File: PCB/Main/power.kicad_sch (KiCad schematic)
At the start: 6 parts

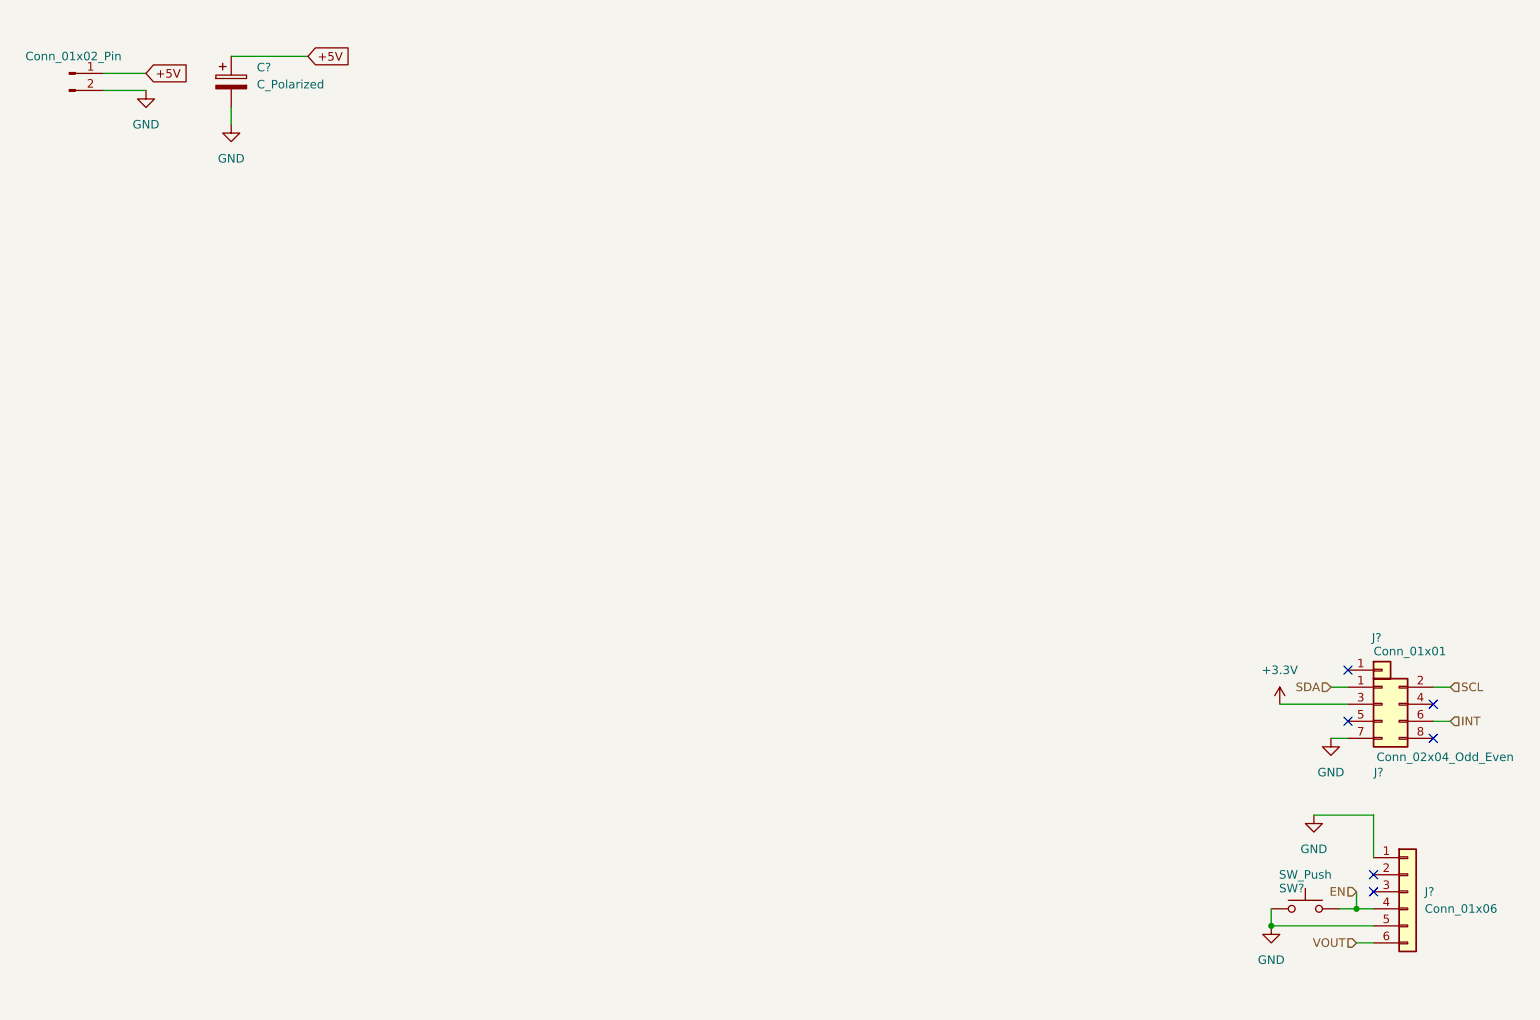
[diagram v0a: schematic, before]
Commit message: renaming y basico sin pcb
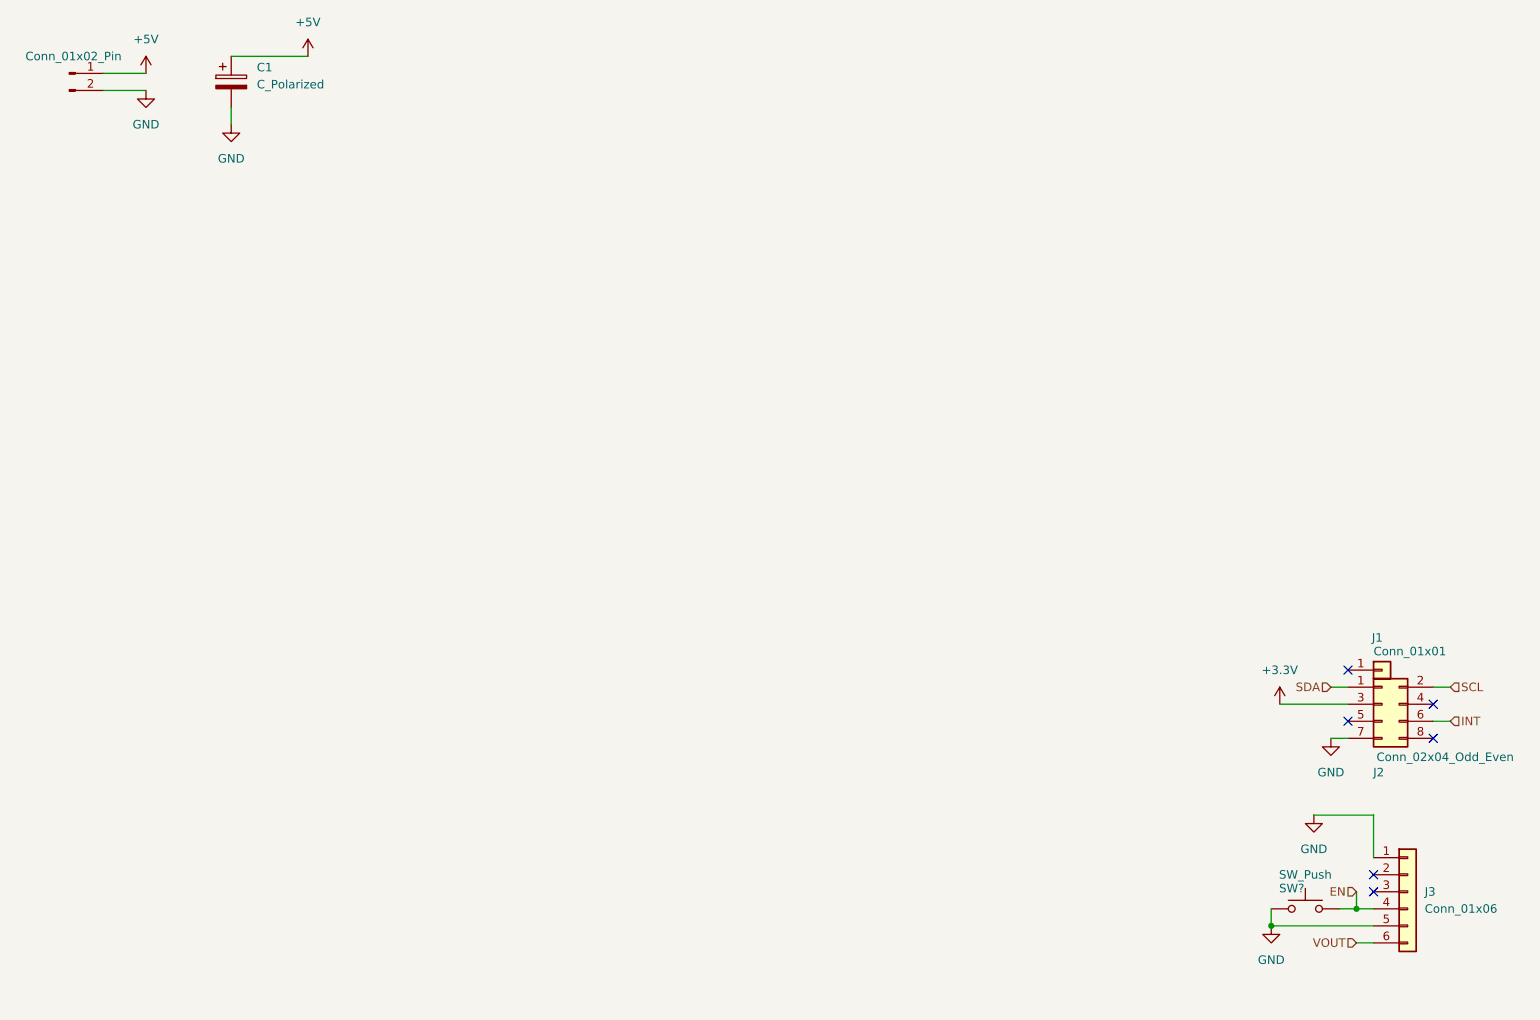
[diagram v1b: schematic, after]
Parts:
- gave numbers to parts that had none: 4
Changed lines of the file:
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@@
-		)
-	)
-	(global_label "+5V"
-		(shape input)
-		(at 68.58 24.13 0)
-		(fields_autoplaced yes)
-		(effects
-			(font
-				(size 1.27 1.27)
-			)
-			(justify left)
-		)
-		(property "Intersheetrefs" "${INTERSHEET_REFS}"
-			(at 75.4357 24.13 0)
-			(effects
-				(font
-					(size 1.27 1.27)
-				)
-				(justify left)
-				(hide yes)
-			)
-		)
-	)
-	(global_label "+5V"
-		(shape input)
-		(at 44.45 26.67 0)
-		(fields_autoplaced yes)
-		(effects
-			(font
-				(size 1.27 1.27)
-			)
-			(justify left)
-		)
-		(property "Intersheetrefs" "${INTERSHEET_REFS}"
-			(at 51.3057 26.67 0)
-			(effects
-				(font
-					(size 1.27 1.27)
-				)
-				(justify left)
-				(hide yes)
-			)
 		)
 	)
@@
 		(dnp no)
 		(fields_autoplaced yes)
-		(property "Reference" "J?"
+		(property "Reference" "J3"
 			(at 234.95 148.5899 0)
 			(effects
@@
 			(project "Main"
 				(path "/dea5ac8e-3e86-4300-9e2e-2676721051d5/57741c9e-edd5-4d78-9bed-1b543f87d51f"
-					(reference "J?")
+					(reference "J3")
+					(unit 1)
+				)
+			)
+		)
+	)
+	(symbol
+		(lib_id "power:+5V")
+		(at 44.45 26.67 0)
+		(unit 1)
+		(exclude_from_sim no)
+		(in_bom yes)
+		(on_board yes)
+		(dnp no)
+		(fields_autoplaced yes)
+		(property "Reference" "#PWR05"
+			(at 44.45 30.48 0)
+			(effects
+				(font
+					(size 1.27 1.27)
+				)
+				(hide yes)
+			)
+		)
+		(property "Value" "+5V"
+			(at 44.45 21.59 0)
+			(effects
+				(font
+					(size 1.27 1.27)
+				)
+			)
+		)
+		(property "Footprint" ""
+			(at 44.45 26.67 0)
+			(effects
+				(font
+					(size 1.27 1.27)
+				)
+				(hide yes)
+			)
+		)
+		(property "Datasheet" ""
+			(at 44.45 26.67 0)
+			(effects
+				(font
+					(size 1.27 1.27)
+				)
+				(hide yes)
+			)
+		)
+		(property "Description" "Power symbol creates a global label with name \"+5V\""
+			(at 44.45 26.67 0)
+			(effects
+				(font
+					(size 1.27 1.27)
+				)
+				(hide yes)
+			)
+		)
+		(pin "1"
+		)
+		(instances
+			(project ""
+				(path "/dea5ac8e-3e86-4300-9e2e-2676721051d5/57741c9e-edd5-4d78-9bed-1b543f87d51f"
+					(reference "#PWR05")
 					(unit 1)
 				)
@@
 		(dnp no)
 		(fields_autoplaced yes)
-		(property "Reference" "C?"
+		(property "Reference" "C1"
 			(at 60.96 25.7809 0)
 			(effects
@@
 			(project "Main"
 				(path "/dea5ac8e-3e86-4300-9e2e-2676721051d5/57741c9e-edd5-4d78-9bed-1b543f87d51f"
-					(reference "C?")
+					(reference "C1")
 					(unit 1)
 				)
@@
 		(on_board yes)
 		(dnp no)
-		(property "Reference" "J?"
+		(property "Reference" "J2"
 			(at 228.092 130.81 0)
 			(effects
@@
 			(project "Main"
 				(path "/dea5ac8e-3e86-4300-9e2e-2676721051d5/57741c9e-edd5-4d78-9bed-1b543f87d51f"
-					(reference "J?")
+					(reference "J2")
 					(unit 1)
 				)
@@
 		(on_board yes)
 		(dnp no)
-		(property "Reference" "J?"
+		(property "Reference" "J1"
 			(at 227.076 110.744 0)
 			(effects
@@
 			(project "Main"
 				(path "/dea5ac8e-3e86-4300-9e2e-2676721051d5/57741c9e-edd5-4d78-9bed-1b543f87d51f"
-					(reference "J?")
+					(reference "J1")
 					(unit 1)
 				)
@@
 					(unit 1)
 				)
+			)
+		)
+	)
+	(symbol
+		(lib_id "power:+5V")
+		(at 68.58 24.13 0)
+		(unit 1)
+		(exclude_from_sim no)
+		(in_bom yes)
+		(on_board yes)
+		(dnp no)
+		(fields_autoplaced yes)
+		(property "Reference" "#PWR06"
+			(at 68.58 27.94 0)
+			(effects
+				(font
+					(size 1.27 1.27)
+				)
+				(hide yes)
+			)
+		)
+		(property "Value" "+5V"
+			(at 68.58 19.05 0)
+			(effects
+				(font
+					(size 1.27 1.27)
+				)
+			)
+		)
+		(property "Footprint" ""
+			(at 68.58 24.13 0)
+			(effects
+				(font
+					(size 1.27 1.27)
+				)
+				(hide yes)
+			)
+		)
+		(property "Datasheet" ""
+			(at 68.58 24.13 0)
+			(effects
+				(font
+					(size 1.27 1.27)
+				)
+				(hide yes)
+			)
+		)
+		(property "Description" "Power symbol creates a global label with name \"+5V\""
+			(at 68.58 24.13 0)
+			(effects
+				(font
+					(size 1.27 1.27)
+				)
+				(hide yes)
+			)
+		)
+		(pin "1"
+		)
+		(instances
+			(project ""
+				(path "/dea5ac8e-3e86-4300-9e2e-2676721051d5/57741c9e-edd5-4d78-9bed-1b543f87d51f"
+					(reference "#PWR06")
+					(unit 1)
+				)

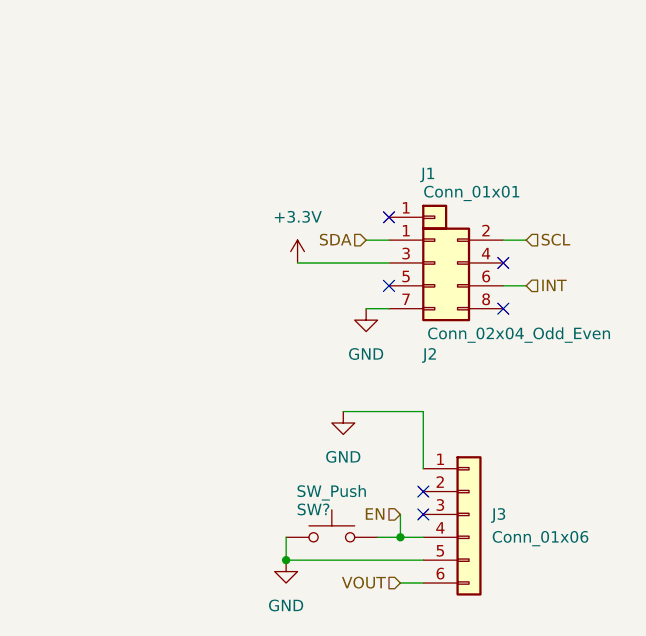
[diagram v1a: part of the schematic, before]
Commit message: rename y conectores
tambien se añaden pours
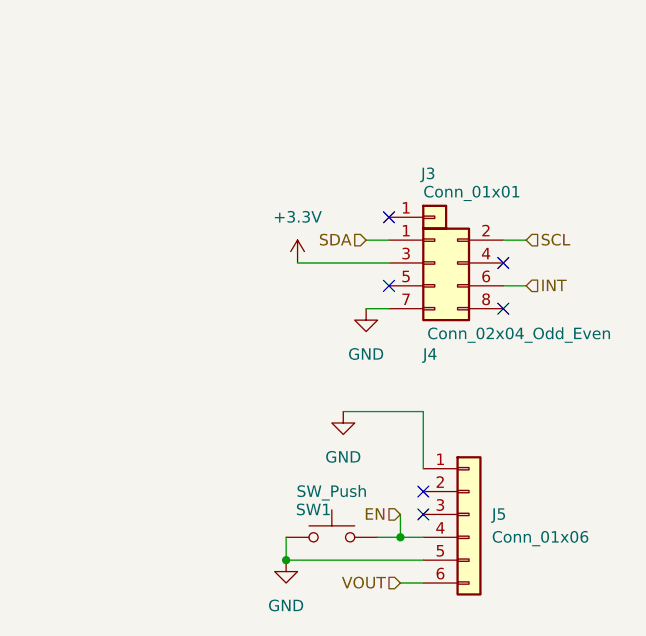
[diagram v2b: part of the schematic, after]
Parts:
- gave numbers to parts that had none: 2
- renumbered J1 to J3, J2 to J4, J3 to J5
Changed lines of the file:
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@@
 		(on_board yes)
 		(dnp no)
-		(property "Reference" "SW?"
+		(property "Reference" "SW1"
 			(at 215.138 148.082 0)
 			(effects
@@
 			(project "Main"
 				(path "/dea5ac8e-3e86-4300-9e2e-2676721051d5/57741c9e-edd5-4d78-9bed-1b543f87d51f"
-					(reference "SW?")
+					(reference "SW1")
 					(unit 1)
 				)
@@
 		(dnp no)
 		(fields_autoplaced yes)
-		(property "Reference" "J3"
+		(property "Reference" "J5"
 			(at 234.95 148.5899 0)
 			(effects
@@
 			(project "Main"
 				(path "/dea5ac8e-3e86-4300-9e2e-2676721051d5/57741c9e-edd5-4d78-9bed-1b543f87d51f"
-					(reference "J3")
+					(reference "J5")
 					(unit 1)
 				)
@@
 		(dnp no)
 		(fields_autoplaced yes)
-		(property "Reference" "#PWR05"
+		(property "Reference" "#PWR08"
 			(at 44.45 30.48 0)
 			(effects
@@
 			(project ""
 				(path "/dea5ac8e-3e86-4300-9e2e-2676721051d5/57741c9e-edd5-4d78-9bed-1b543f87d51f"
-					(reference "#PWR05")
+					(reference "#PWR08")
 					(unit 1)
 				)
@@
 		(on_board yes)
 		(dnp no)
-		(property "Reference" "J?"
+		(property "Reference" "J2"
 			(at 33.655 21.59 0)
 			(effects
@@
 			(project "Main"
 				(path "/dea5ac8e-3e86-4300-9e2e-2676721051d5/57741c9e-edd5-4d78-9bed-1b543f87d51f"
-					(reference "J?")
+					(reference "J2")
 					(unit 1)
 				)
@@
 		(dnp no)
 		(fields_autoplaced yes)
-		(property "Reference" "#PWR?"
+		(property "Reference" "#PWR010"
 			(at 57.15 40.64 0)
 			(effects
@@
 			(project "Main"
 				(path "/dea5ac8e-3e86-4300-9e2e-2676721051d5/57741c9e-edd5-4d78-9bed-1b543f87d51f"
-					(reference "#PWR?")
+					(reference "#PWR010")
 					(unit 1)
 				)
@@
 		(dnp no)
 		(fields_autoplaced yes)
-		(property "Reference" "#PWR?"
+		(property "Reference" "#PWR015"
 			(at 220.98 132.08 0)
 			(effects
@@
 			(project "Main"
 				(path "/dea5ac8e-3e86-4300-9e2e-2676721051d5/57741c9e-edd5-4d78-9bed-1b543f87d51f"
-					(reference "#PWR?")
+					(reference "#PWR015")
 					(unit 1)
 				)
@@
 		(on_board yes)
 		(dnp no)
-		(property "Reference" "J2"
+		(property "Reference" "J4"
 			(at 228.092 130.81 0)
 			(effects
@@
 			(project "Main"
 				(path "/dea5ac8e-3e86-4300-9e2e-2676721051d5/57741c9e-edd5-4d78-9bed-1b543f87d51f"
-					(reference "J2")
+					(reference "J4")
 					(unit 1)
 				)
@@
 		(on_board yes)
 		(dnp no)
-		(property "Reference" "J1"
+		(property "Reference" "J3"
 			(at 227.076 110.744 0)
 			(effects
@@
 			(project "Main"
 				(path "/dea5ac8e-3e86-4300-9e2e-2676721051d5/57741c9e-edd5-4d78-9bed-1b543f87d51f"
-					(reference "J1")
+					(reference "J3")
 					(unit 1)
 				)
@@
 		(on_board yes)
 		(dnp no)
-		(property "Reference" "#PWR?"
+		(property "Reference" "#PWR09"
 			(at 44.45 35.56 0)
 			(effects
@@
 			(project "Main"
 				(path "/dea5ac8e-3e86-4300-9e2e-2676721051d5/57741c9e-edd5-4d78-9bed-1b543f87d51f"
-					(reference "#PWR?")
+					(reference "#PWR09")
 					(unit 1)
 				)
@@
 		(dnp no)
 		(fields_autoplaced yes)
-		(property "Reference" "#PWR06"
+		(property "Reference" "#PWR011"
 			(at 68.58 27.94 0)
 			(effects
@@
 			(project ""
 				(path "/dea5ac8e-3e86-4300-9e2e-2676721051d5/57741c9e-edd5-4d78-9bed-1b543f87d51f"
-					(reference "#PWR06")
+					(reference "#PWR011")
 					(unit 1)
 				)
@@
 		(dnp no)
 		(fields_autoplaced yes)
-		(property "Reference" "#PWR?"
+		(property "Reference" "#PWR014"
 			(at 218.44 143.51 0)
 			(effects
@@
 			(project "Main"
 				(path "/dea5ac8e-3e86-4300-9e2e-2676721051d5/57741c9e-edd5-4d78-9bed-1b543f87d51f"
-					(reference "#PWR?")
+					(reference "#PWR014")
 					(unit 1)
 				)
@@
 		(dnp no)
 		(fields_autoplaced yes)
-		(property "Reference" "#PWR?"
+		(property "Reference" "#PWR013"
 			(at 213.36 124.46 0)
 			(effects
@@
 			(project "Main"
 				(path "/dea5ac8e-3e86-4300-9e2e-2676721051d5/57741c9e-edd5-4d78-9bed-1b543f87d51f"
-					(reference "#PWR?")
+					(reference "#PWR013")
 					(unit 1)
 				)
@@
 		(dnp no)
 		(fields_autoplaced yes)
-		(property "Reference" "#PWR?"
+		(property "Reference" "#PWR012"
 			(at 212.09 160.02 0)
 			(effects
@@
 			(project "Main"
 				(path "/dea5ac8e-3e86-4300-9e2e-2676721051d5/57741c9e-edd5-4d78-9bed-1b543f87d51f"
-					(reference "#PWR?")
-					(unit 1)
-				)
+					(reference "#PWR012")
+					(unit 1)
+				)

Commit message: pcb continued
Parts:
- C1: value C_Polarized -> 470µF; footprint (none) -> Capacitor_Tantalum_SMD:CP_EIA-7343-31_Kemet-D
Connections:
- net +5V: no longer C1.1
- net GND: no longer C1.2, J2.2 (Pin_2), J5.1 (Pin_1), J5.5 (Pin_5), SW1.1
- net VOUT renamed POWER_5V
- net POWER_5V: now also C1.1
- new net POWER_GND: C1.2, J2.2 (Pin_2), J5.1 (Pin_1), J5.5 (Pin_5), SW1.1

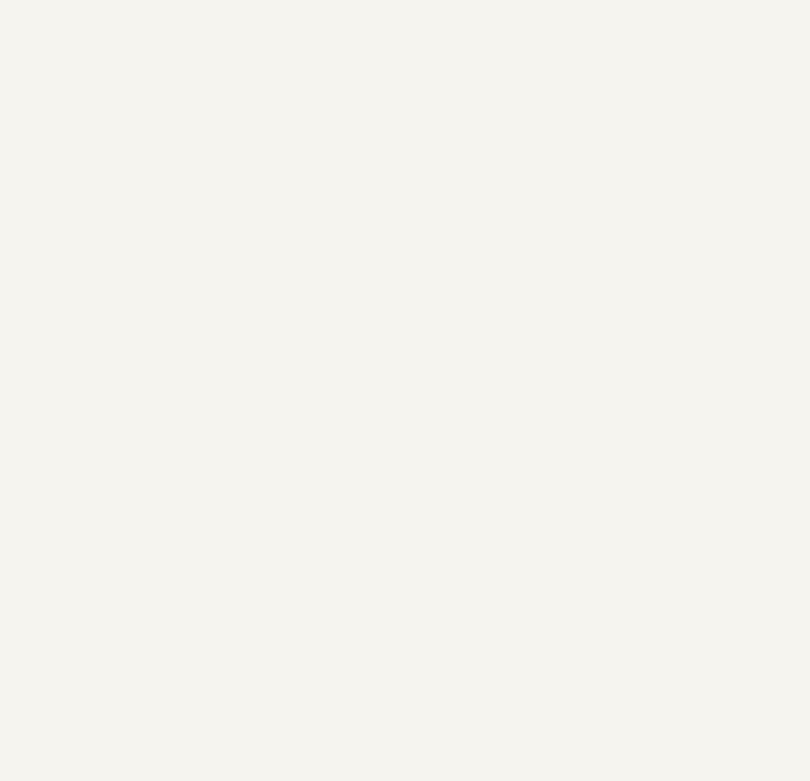
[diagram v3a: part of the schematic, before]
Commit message: power with ampripper
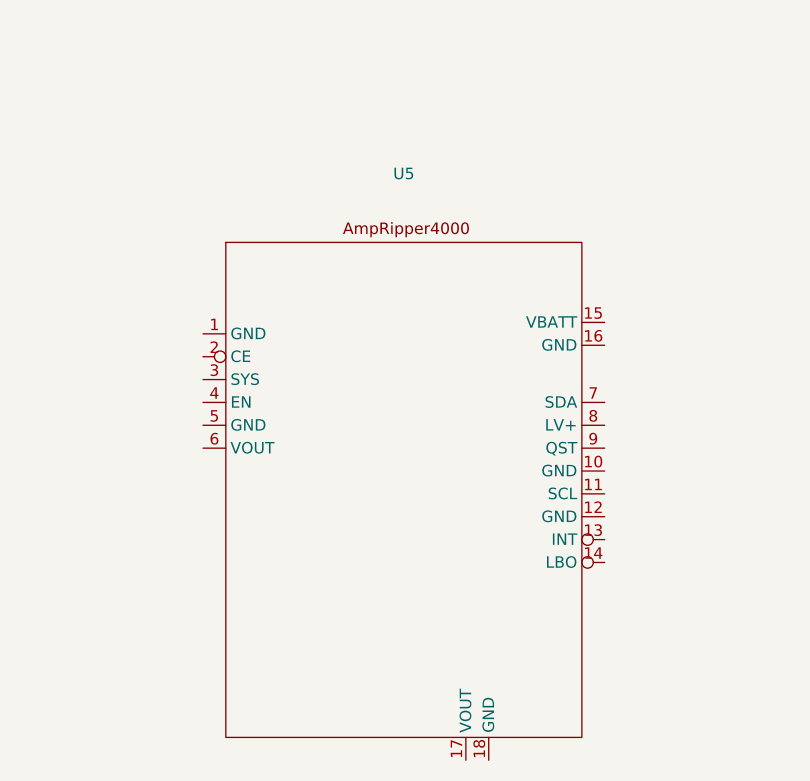
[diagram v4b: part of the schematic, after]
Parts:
- added U5: ~, symbol Ampripper4000:AmpRipper4000
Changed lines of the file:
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@@
+	)
+	(symbol
+		(lib_id "Ampripper4000:AmpRipper4000")
+		(at 78.74 107.95 0)
+		(unit 1)
+		(exclude_from_sim no)
+		(in_bom yes)
+		(on_board yes)
+		(dnp no)
+		(fields_autoplaced yes)
+		(property "Reference" "U5"
+			(at 98.52 100.33 0)
+			(effects
+				(font
+					(size 1.27 1.27)
+				)
+			)
+		)
+		(property "Value" "~"
+			(at 98.52 102.87 0)
+			(effects
+				(font
+					(size 1.27 1.27)
+				)
+			)
+		)
+		(property "Footprint" ""
+			(at 78.74 107.95 0)
+			(effects
+				(font
+					(size 1.27 1.27)
+				)
+				(hide yes)
+			)
+		)
+		(property "Datasheet" ""
+			(at 78.74 107.95 0)
+			(effects
+				(font
+					(size 1.27 1.27)
+				)
+				(hide yes)
+			)
+		)
+		(property "Description" ""
+			(at 78.74 107.95 0)
+			(effects
+				(font
+					(size 1.27 1.27)
+				)
+				(hide yes)
+			)
+		)
+		(pin "14"
+		)
+		(pin "18"
+		)
+		(pin "9"
+		)
+		(pin "16"
+		)
+		(pin "15"
+		)
+		(pin "8"
+		)
+		(pin "17"
+		)
+		(pin "11"
+		)
+		(pin "13"
+		)
+		(pin "7"
+		)
+		(pin "1"
+		)
+		(pin "2"
+		)
+		(pin "3"
+		)
+		(pin "4"
+		)
+		(pin "5"
+		)
+		(pin "6"
+		)
+		(pin "12"
+		)
+		(pin "10"
+		)
+		(instances
+			(project ""
+				(path "/dea5ac8e-3e86-4300-9e2e-2676721051d5/57741c9e-edd5-4d78-9bed-1b543f87d51f"
+					(reference "U5")
+					(unit 1)
+				)
+			)
+		)
 	)
 	(symbol
